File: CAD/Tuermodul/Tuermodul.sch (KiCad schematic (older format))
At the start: 52 parts, among them J101 Conn_02x16_Counter_Clockwise, U101 93LC46B, U102 74HC595, U103 FT4232H, U104 MCP1825S, Y101 12MHz

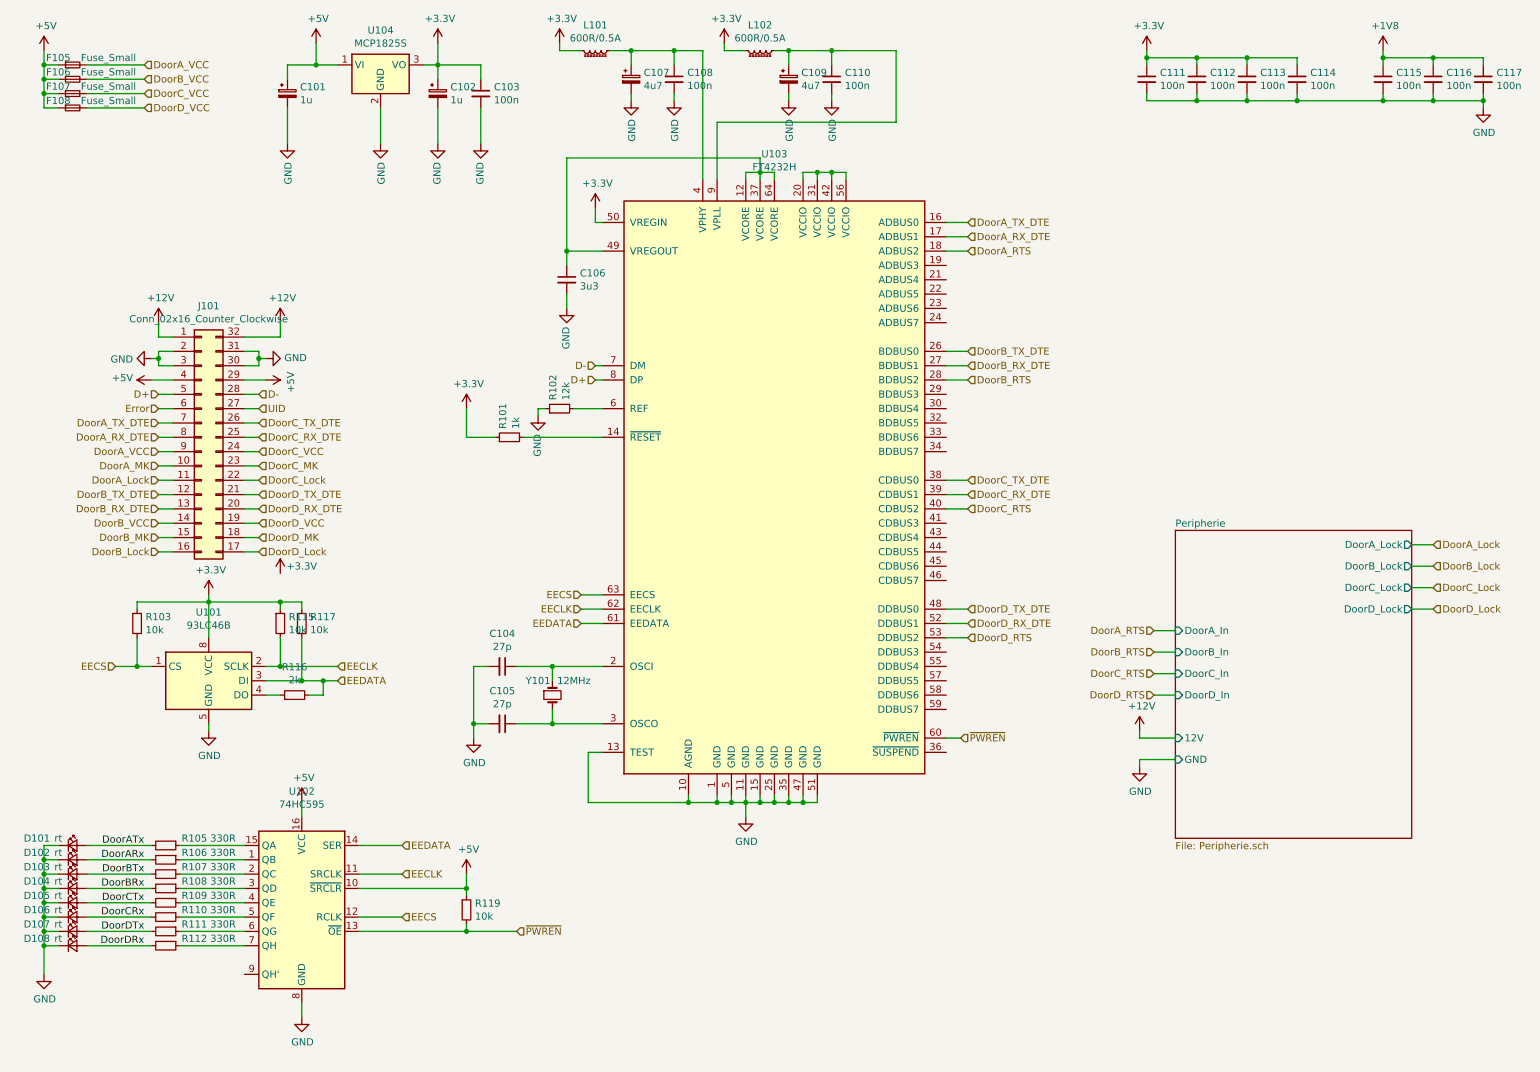
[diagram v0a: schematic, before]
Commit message: -add: Fuse Error, missing LEDs -mod: some Resistor footprints changed -mod: first placement in layout
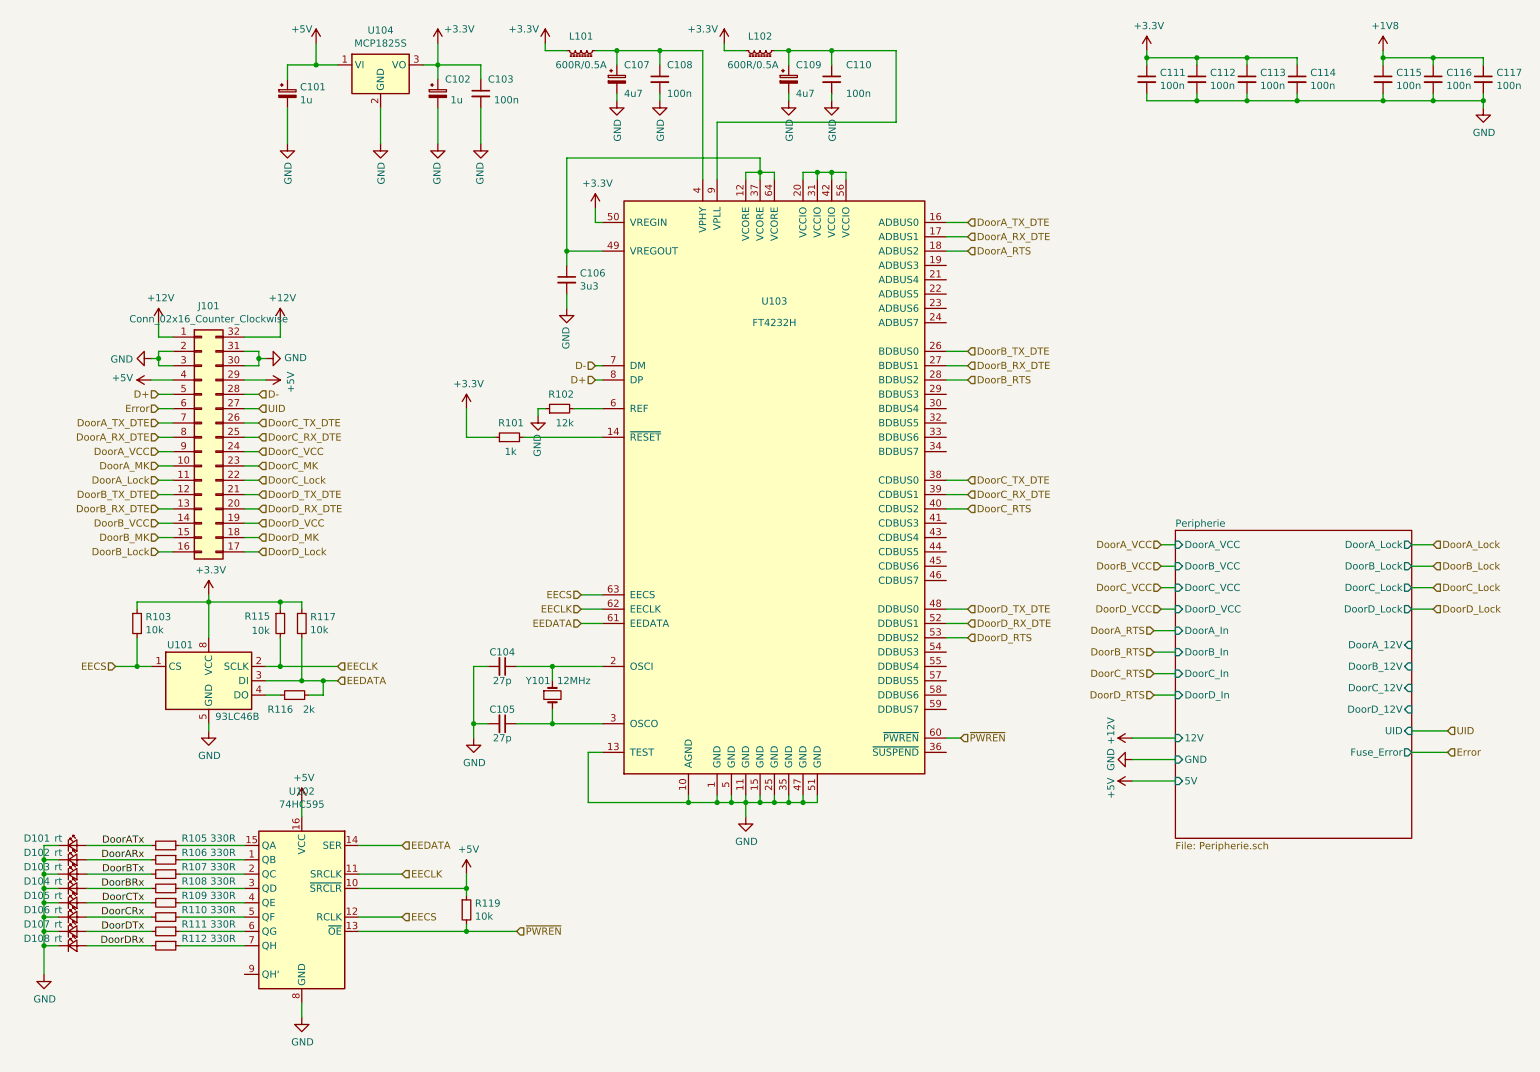
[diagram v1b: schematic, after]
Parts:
- removed F105, F106, F107, F108: Fuse_Small, Fuse:Fuseholder_Cylinder-5x20mm_Schurter_0031_8201_Horizontal_Open, symbol Device:Fuse_Small
- R101, R102, R103, R115, R116, R117, R119: footprint Resistor_THT:R_Axial_DIN0207_L6.3mm_D2.5mm_P7.62mm_Horizontal -> Resistor_SMD:R_0603_1608Metric_Pad1.05x0.95mm_HandSolder
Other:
- moved on the sheet: C107, C108, L101

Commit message: -add: Front.sch for front panel -mod: moved leds and switches to front panel -mod: added MK contacts (not finished jet) -mod: added switches
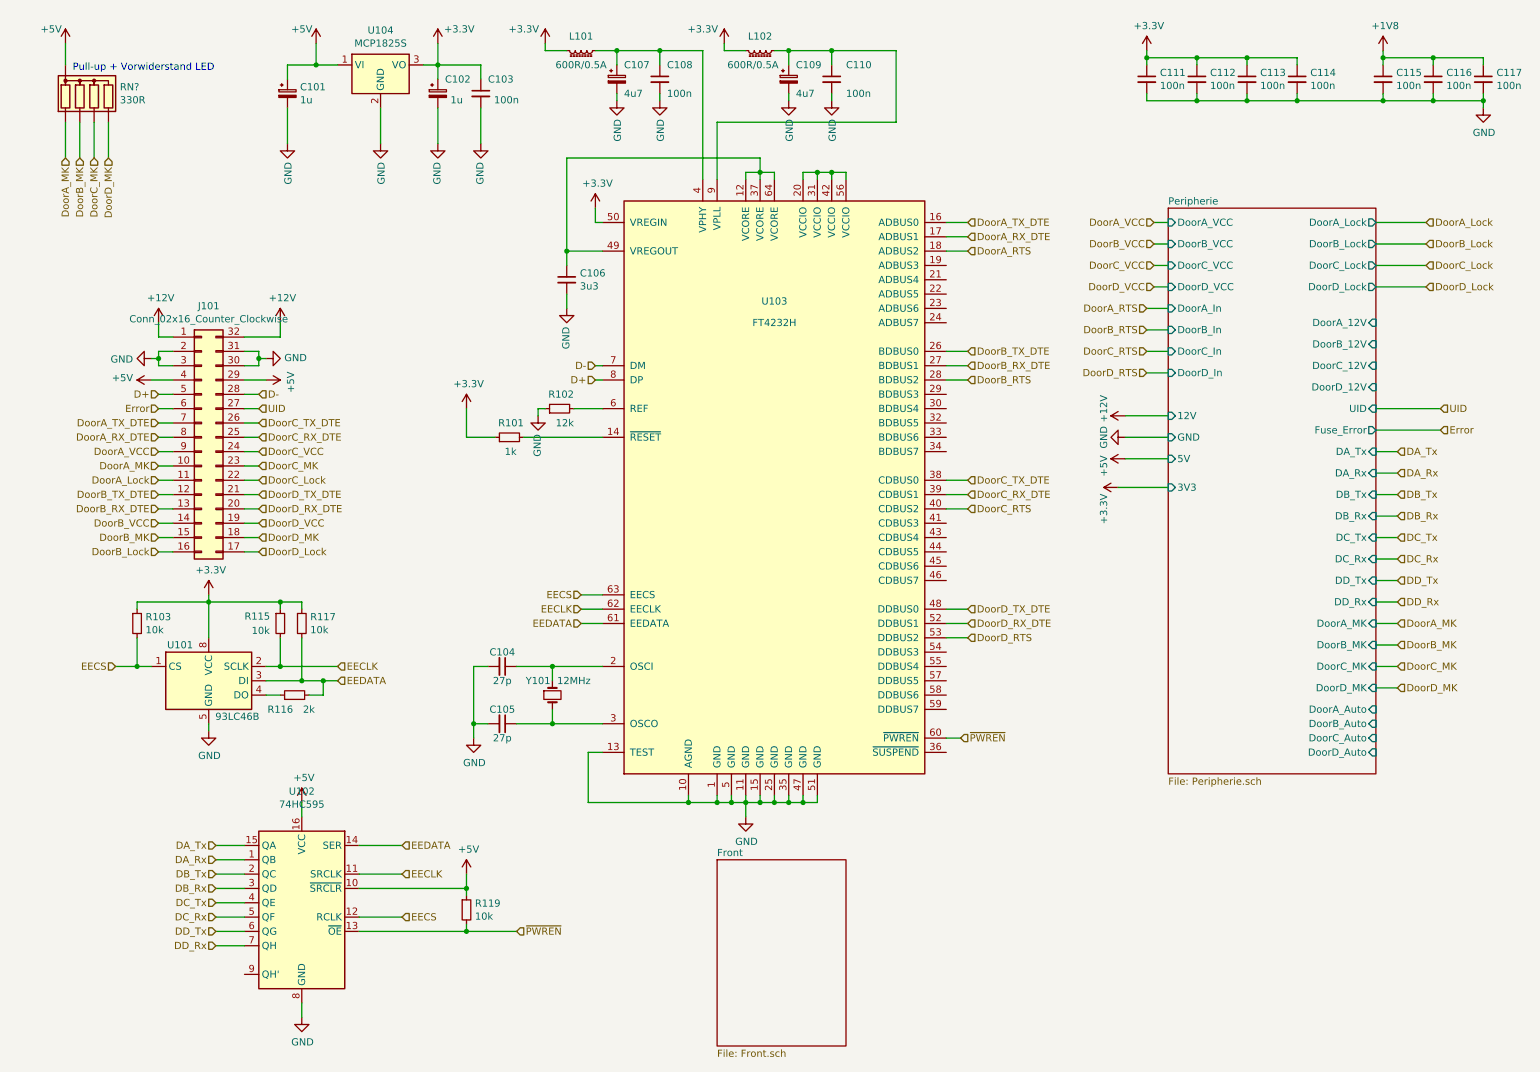
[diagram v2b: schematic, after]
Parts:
- removed D101, D102, D103, D104, D105, D106, D107, D108: rt, LED_THT:LED_D3.0mm, symbol Device:LED_Small
- removed R105, R106, R107, R108, R109, R110, R111, R112: 330R, Resistor_THT:R_Axial_DIN0207_L6.3mm_D2.5mm_P7.62mm_Horizontal, symbol Device:R_Small
- added RN?: 330R, Resistor_THT:R_Array_SIP5, symbol Device:R_Network04
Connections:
- net +5V: now also RN?.1 (common)
- net DoorA_MK: now also RN?.2 (R1)
- net DoorB_MK: now also RN?.3 (R2)
- net DoorC_MK: now also RN?.4 (R3)
- net DoorD_MK: now also RN?.5 (R4)
- net DA_Rx: now reaches U102.1 (QB)
- net DA_Tx: now reaches U102.15 (QA)
- net DB_Tx: now reaches U102.2 (QC)
- net DB_Rx: now reaches U102.3 (QD)
- net DC_Tx: now reaches U102.4 (QE)
- net DC_Rx: now reaches U102.5 (QF)
- net DD_Tx: now reaches U102.6 (QG)
- net DD_Rx: now reaches U102.7 (QH)
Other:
- note added: "Pull-up + Vorwiderstand LED"

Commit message: -add: switch library for spdt switches -mod: improvements in schematic, bugfixes -mod: placement and routing of the ftdi chip + chicken food
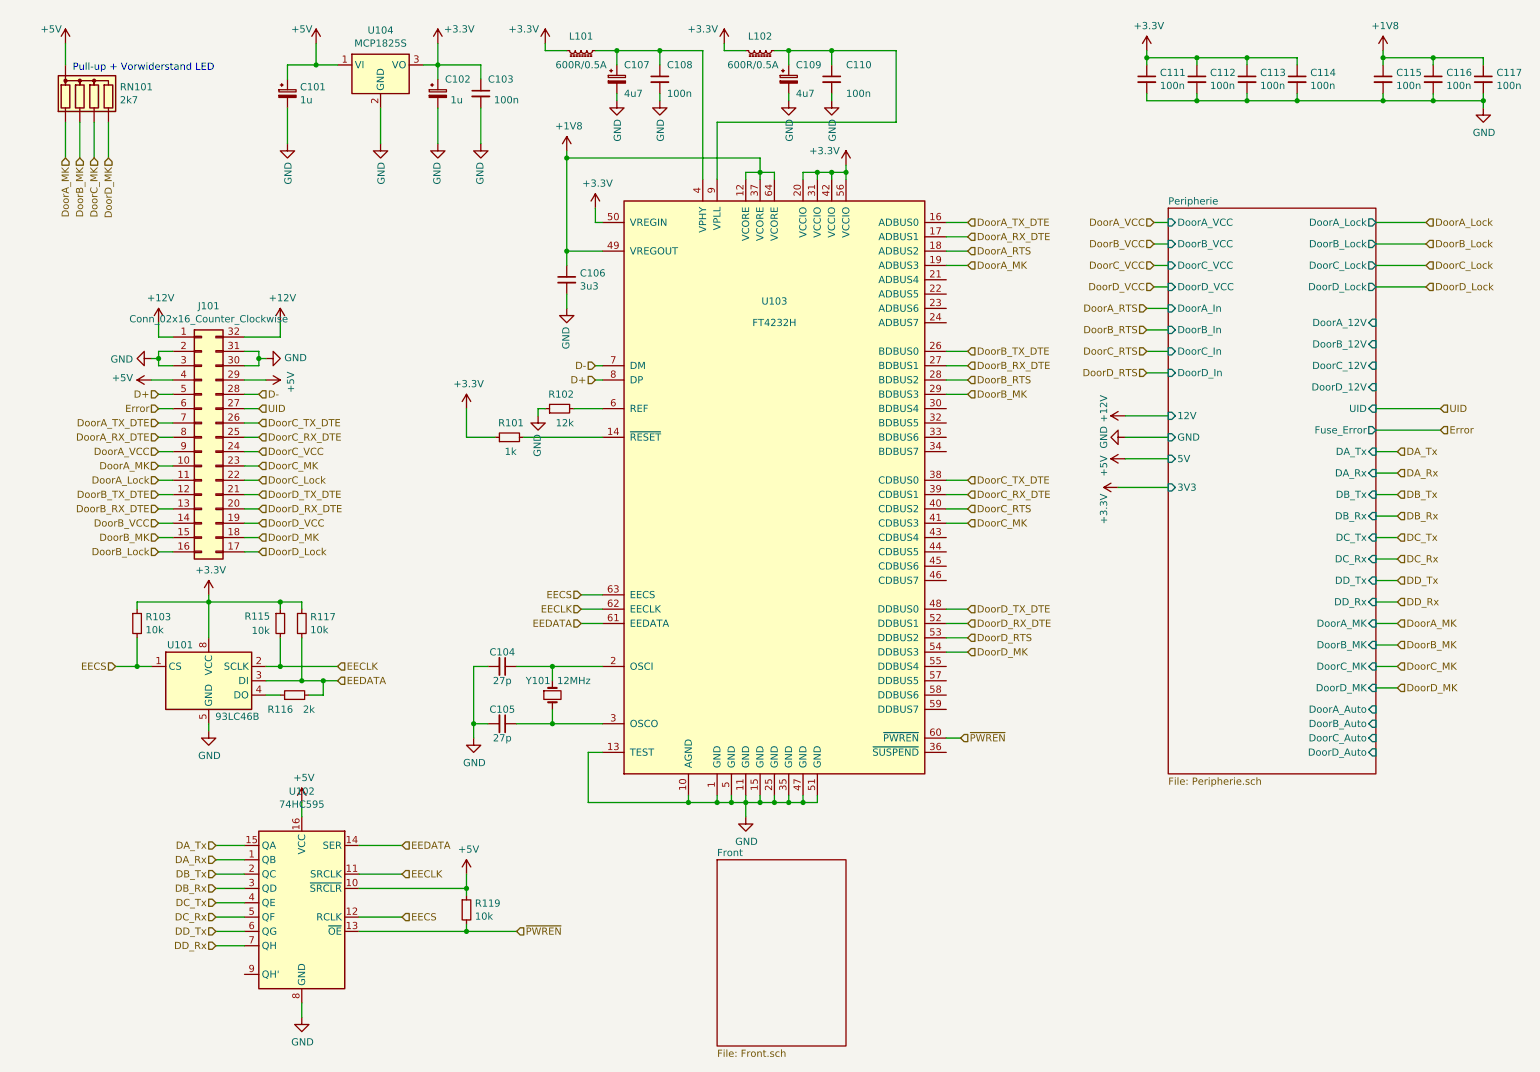
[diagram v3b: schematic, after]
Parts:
- RN101: renamed from RN?; value 330R -> 2k7
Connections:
- net +1V8: now also C106.1, U103.12 (VCORE), U103.37 (VCORE), U103.49 (VREGOUT), U103.64 (VCORE)
- net +3V3: now also U103.20 (VCCIO), U103.31 (VCCIO), U103.42 (VCCIO), U103.56 (VCCIO)
- net DoorA_MK: now also U103.19 (ADBUS3)
- net DoorB_MK: now also U103.29 (BDBUS3)
- net DoorC_MK: now also U103.41 (CDBUS3)
- net DoorD_MK: now also U103.54 (DDBUS3)
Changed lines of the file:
@@
 DoorD_MK
 $Comp
-L Device:R_Network04 RN?
+L Device:R_Network04 RN101
 U 1 1 5C769116
 P 1000 1000
-F 0 "RN?" H 1180 1046 50  0000 L CNN
-F 1 "330R" H 1180 955 50  0000 L CNN
+F 0 "RN101" H 1180 1046 50  0000 L CNN
+F 1 "2k7" H 1180 955 50  0000 L CNN
 F 2 "Resistor_THT:R_Array_SIP5" V 1275 1000 50  0001 C CNN
 F 3 "http://www.vishay.com/docs/31509/csc.pdf" H 1000 1000 50  0001 C CNN
@@
 $EndComp
 $Comp
-L power:+5V #PWR?
+L power:+5V #PWR0111
 U 1 1 5C769345
 P 800 650
-F 0 "#PWR?" H 800 500 50  0001 C CNN
+F 0 "#PWR0111" H 800 500 50  0001 C CNN
 F 1 "+5V" H 700 750 50  0000 C CNN
 F 2 "" H 800 650 50  0001 C CNN
@@
 Text Notes 850  850  0    50   ~ 0
 Pull-up + Vorwiderstand LED
+Wire Wire Line
+	7100 2200 6950 2200
+Wire Wire Line
+	7100 3100 6950 3100
+Wire Wire Line
+	7100 4000 6950 4000
+Wire Wire Line
+	7100 4900 6950 4900
+Text HLabel 7100 2200 2    50   Input ~ 0
+DoorA_MK
+Text HLabel 7100 3100 2    50   Input ~ 0
+DoorB_MK
+Text HLabel 7100 4000 2    50   Input ~ 0
+DoorC_MK
+Text HLabel 7100 4900 2    50   Input ~ 0
+DoorD_MK
+$Comp
+L power:+3.3V #PWR?
+U 1 1 5C607DE2
+P 6250 1500
+F 0 "#PWR?" H 6250 1350 50  0001 C CNN
+F 1 "+3.3V" H 6100 1600 50  0000 C CNN
+F 2 "" H 6250 1500 50  0001 C CNN
+F 3 "" H 6250 1500 50  0001 C CNN
+	1    6250 1500
+	1    0    0    -1
+$EndComp
+Wire Wire Line
+	6250 1500 6250 1550
+Connection ~ 6250 1550
+$Comp
+L power:+1V8 #PWR?
+U 1 1 5C618DD8
+P 4300 1400
+F 0 "#PWR?" H 4300 1250 50  0001 C CNN
+F 1 "+1V8" H 4315 1573 50  0000 C CNN
+F 2 "" H 4300 1400 50  0001 C CNN
+F 3 "" H 4300 1400 50  0001 C CNN
+	1    4300 1400
+	1    0    0    -1
+$EndComp
+Wire Wire Line
+	4300 1400 4300 1450
+Connection ~ 4300 1450
 $EndSCHEMATC

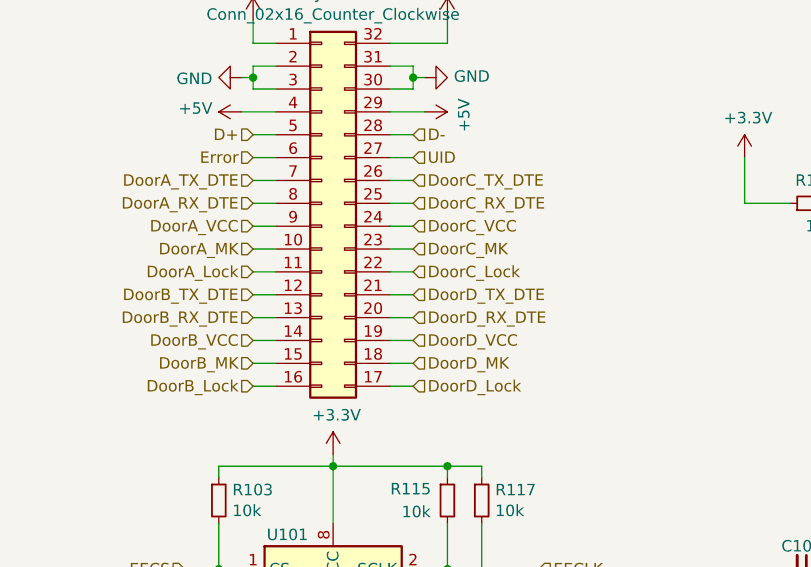
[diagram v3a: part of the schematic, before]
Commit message: -mod: layout tuermodul
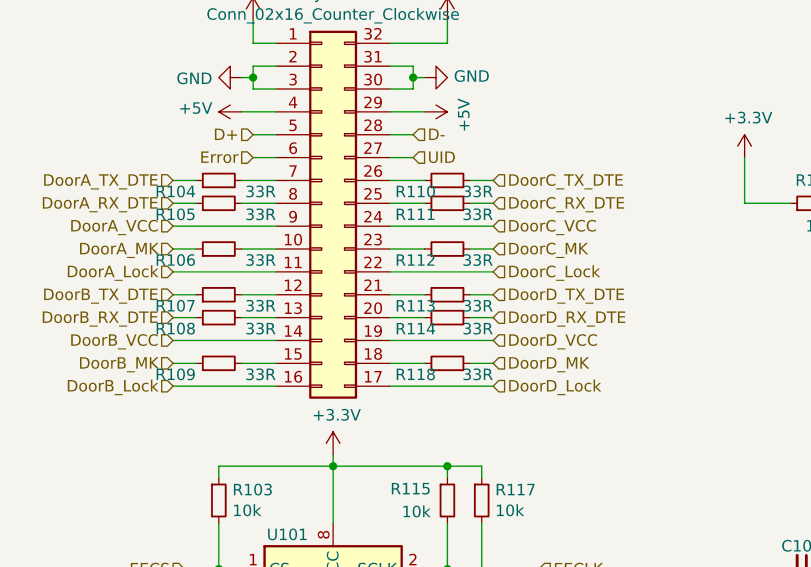
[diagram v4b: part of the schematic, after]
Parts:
- added R104, R105, R106, R107, R108, R109, R110, R111, R112, R113, R114, R118: 33R, Resistor_SMD:R_0603_1608Metric_Pad1.05x0.95mm_HandSolder, symbol Device:R_Small
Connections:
- net DoorA_MK: now also R106.1; no longer J101.10 (Pin_10)
- net DoorA_RX_DTE: now also R105.1; no longer J101.8 (Pin_8)
- net DoorA_TX_DTE: now also R104.1; no longer J101.7 (Pin_7)
- net DoorB_MK: now also R109.1; no longer J101.15 (Pin_15)
- net DoorB_RX_DTE: now also R108.1; no longer J101.13 (Pin_13)
- net DoorB_TX_DTE: now also R107.1; no longer J101.12 (Pin_12)
- net DoorC_MK: now also R112.2; no longer J101.23 (Pin_23)
- net DoorC_RX_DTE: now also R111.2; no longer J101.25 (Pin_25)
- net DoorC_TX_DTE: now also R110.2; no longer J101.26 (Pin_26)
- net DoorD_MK: now also R118.2; no longer J101.18 (Pin_18)
- net DoorD_RX_DTE: now also R114.2; no longer J101.20 (Pin_20)
- net DoorD_TX_DTE: now also R113.2; no longer J101.21 (Pin_21)
- new net: J101.10 (Pin_10), R106.2
- new net: J101.12 (Pin_12), R107.2
- new net: J101.13 (Pin_13), R108.2
- new net: J101.15 (Pin_15), R109.2
- new net: J101.18 (Pin_18), R118.1
- new net: J101.20 (Pin_20), R114.1
- new net: J101.21 (Pin_21), R113.1
- new net: J101.23 (Pin_23), R112.1
- new net: J101.25 (Pin_25), R111.1
- new net: J101.26 (Pin_26), R110.1
- new net: J101.7 (Pin_7), R104.2
- new net: J101.8 (Pin_8), R105.2

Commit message: -mod: adapted TechSpec due to power enable discussion -mod: changed pin header for front-to-main panel connection -mod: general layout work
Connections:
- net UID renamed ~PWR_EN~
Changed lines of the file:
@@
 D-
 Text HLabel 2150 3200 2    50   Input ~ 0
-UID
+~PWR_EN~
 Text HLabel 2500 3300 2    50   Input ~ 0
 DoorC_TX_DTE
@@
 F18 "DoorC_VCC" I L 8500 2200 50
 F19 "DoorD_VCC" I L 8500 2350 50
-F20 "UID" I R 9950 3200 50
-F21 "Fuse_Error" O R 9950 3350 50
-F22 "5V" I L 8500 3550 50
-F23 "DA_Tx" I R 9950 3500 50
-F24 "DA_Rx" I R 9950 3650 50
-F25 "DB_Tx" I R 9950 3800 50
-F26 "DB_Rx" I R 9950 3950 50
-F27 "DC_Tx" I R 9950 4100 50
-F28 "DC_Rx" I R 9950 4250 50
-F29 "DD_Tx" I R 9950 4400 50
-F30 "DD_Rx" I R 9950 4550 50
-F31 "DoorA_MK" I R 9950 4700 50
-F32 "DoorB_MK" I R 9950 4850 50
-F33 "DoorC_MK" I R 9950 5000 50
-F34 "DoorD_MK" I R 9950 5150 50
-F35 "DoorA_Auto" I R 9950 5300 50
-F36 "DoorB_Auto" I R 9950 5400 50
-F37 "DoorC_Auto" I R 9950 5500 50
-F38 "DoorD_Auto" I R 9950 5600 50
-F39 "3V3" I L 8500 3750 50
+F20 "Fuse_Error" O R 9950 3350 50
+F21 "5V" I L 8500 3550 50
+F22 "DA_Tx" I R 9950 3500 50
+F23 "DA_Rx" I R 9950 3650 50
+F24 "DB_Tx" I R 9950 3800 50
+F25 "DB_Rx" I R 9950 3950 50
+F26 "DC_Tx" I R 9950 4100 50
+F27 "DC_Rx" I R 9950 4250 50
+F28 "DD_Tx" I R 9950 4400 50
+F29 "DD_Rx" I R 9950 4550 50
+F30 "DoorA_MK" I R 9950 4700 50
+F31 "DoorB_MK" I R 9950 4850 50
+F32 "DoorC_MK" I R 9950 5000 50
+F33 "DoorD_MK" I R 9950 5150 50
+F34 "DoorA_Auto" I R 9950 5300 50
+F35 "DoorB_Auto" I R 9950 5400 50
+F36 "DoorC_Auto" I R 9950 5500 50
+F37 "DoorD_Auto" I R 9950 5600 50
+F38 "3V3" I L 8500 3750 50
+F39 "~PWR_EN~" I R 9950 3200 50
 $EndSheet
 Wire Wire Line
@@
 Text HLabel 10400 3350 2    50   Input ~ 0
 Error
-Text HLabel 10400 3200 2    50   Input ~ 0
-UID
 Wire Wire Line
 	8200 3400 8500 3400
@@
 Wire Wire Line
 	1200 4100 1100 4100
+Text HLabel 10400 3200 2    50   Input ~ 0
+~PWR_EN~
 $EndSCHEMATC
